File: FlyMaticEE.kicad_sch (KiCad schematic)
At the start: 1 part, among them U1 RASPBERRY_PI_4B_4GB

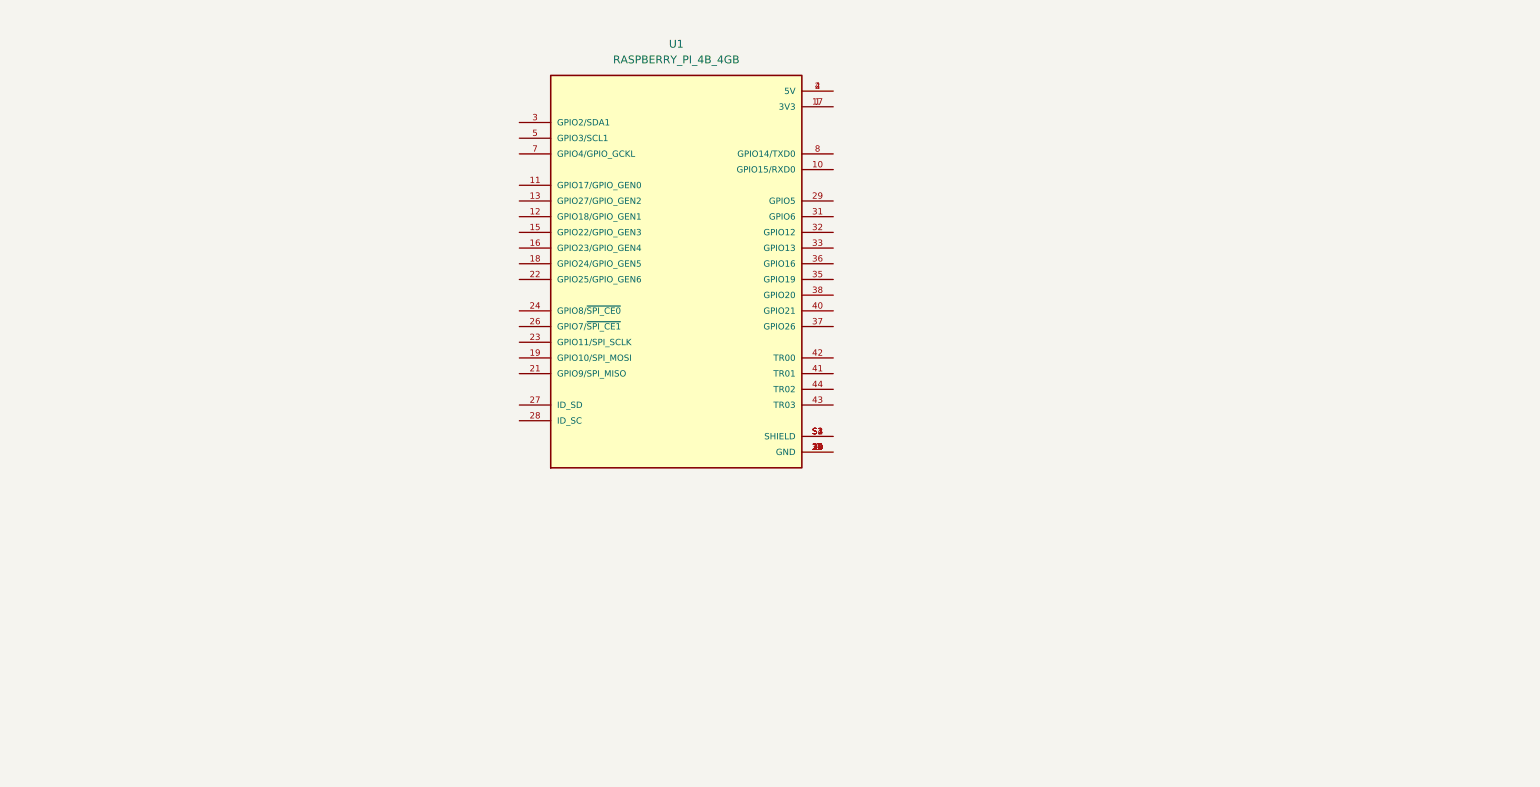
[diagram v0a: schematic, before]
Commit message: Add basic components to the schematic
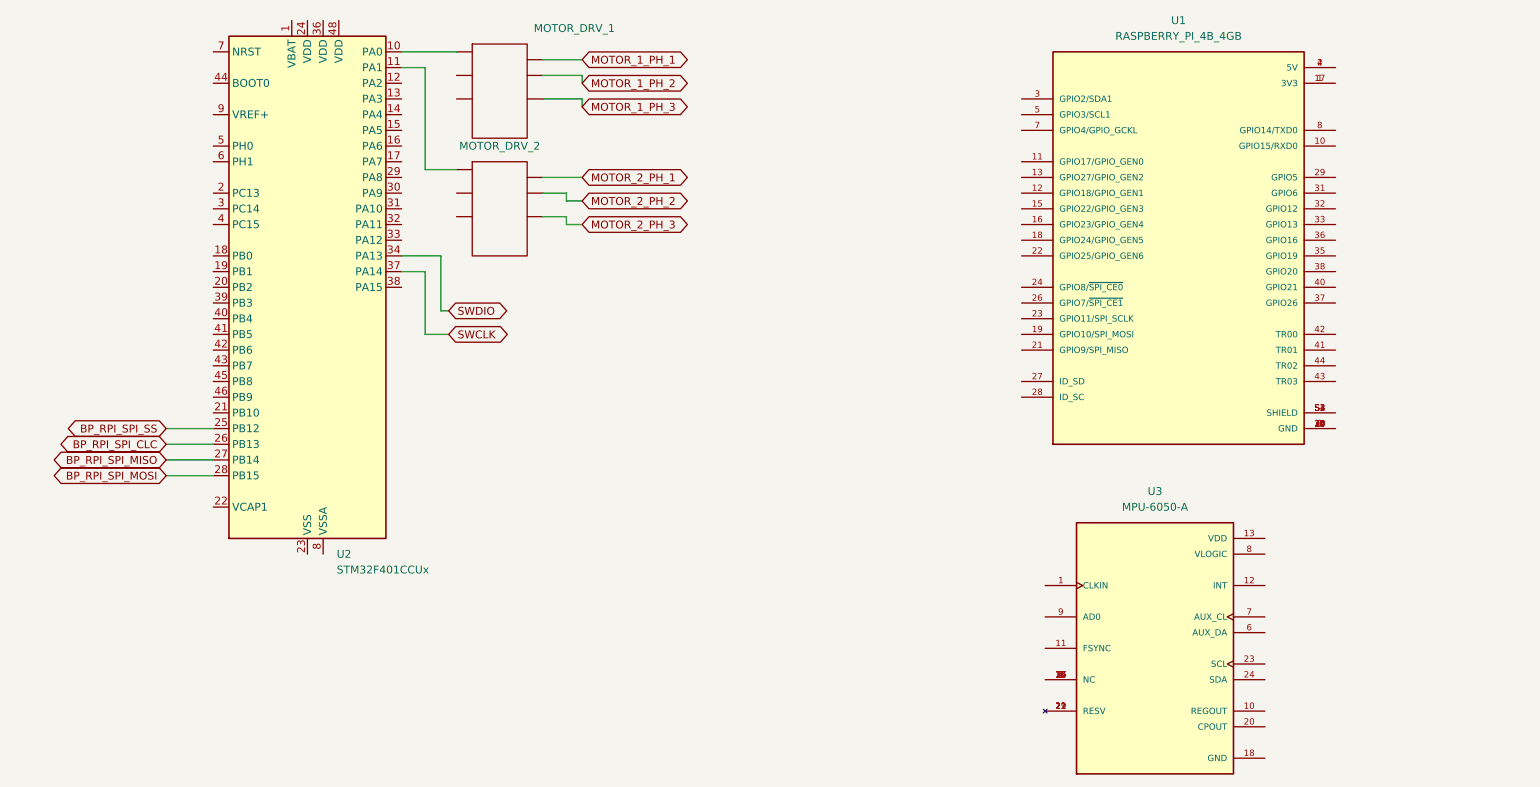
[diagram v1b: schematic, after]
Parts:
- added MOTOR_DRV_1, MOTOR_DRV_2: ~, symbol Driver_Motor:Brushless_ESC_20A_2-3S
- added U2: STM32F401CCUx, Package_DFN_QFN:QFN-48-1EP_7x7mm_P0.5mm_EP5.6x5.6mm, symbol MCU_ST_STM32F4:STM32F401CCUx
- added U3: MPU-6050-A, MPU-6050-A:QFN50P400X400X95-24N, symbol MPU-6050-A:MPU-6050-A
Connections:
- new net: U3.14 (NC), U3.15 (NC), U3.16 (NC), U3.17 (NC), U3.2 (NC), U3.3 (NC), U3.4 (NC), U3.5 (NC)
- new net: U3.19 (RESV), U3.21 (RESV), U3.22 (RESV)
- new net: MOTOR_DRV_1., U2.10 (PA0)
- new net: MOTOR_DRV_2., U2.11 (PA1)
- new net: U2.23 (VSS), U2.35 (VSS), U2.47 (VSS), U2.49 (VSS)
- new net BP_RPI_SPI_CLC: U2.26 (PB13)
- new net BP_RPI_SPI_MISO: U2.27 (PB14)
- new net BP_RPI_SPI_MOSI: U2.28 (PB15)
- new net BP_RPI_SPI_SS: U2.25 (PB12)
- new net MOTOR_1_PH_1: MOTOR_DRV_1.
- new net MOTOR_1_PH_2: MOTOR_DRV_1.
- new net MOTOR_1_PH_3: MOTOR_DRV_1.
- new net MOTOR_2_PH_1: MOTOR_DRV_2.
- new net MOTOR_2_PH_2: MOTOR_DRV_2.
- new net MOTOR_2_PH_3: MOTOR_DRV_2.
- new net SWCLK: U2.37 (PA14)
- new net SWDIO: U2.34 (PA13)
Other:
- moved on the sheet: U1

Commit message: Add pdf schematic to the project
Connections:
- net BP_RPI_SPI_CLC: now also U1.23 (GPIO11/SPI_SCLK)
- net BP_RPI_SPI_MISO: now also U1.21 (GPIO9/SPI_MISO)
- net BP_RPI_SPI_MOSI: now also U1.19 (GPIO10/SPI_MOSI)
- net BP_RPI_SPI_SS: now also U1.24 (GPIO8/~{SPI_CE0})
- net at U3.23 (SCL): now also U1.5 (GPIO3/SCL1)
- net at U3.24 (SDA): now also U1.3 (GPIO2/SDA1)
- net at U1.1 (3V3): no longer U1.17 (3V3)
- net at U1.2 (5V): no longer U1.4 (5V)
- net at U1.S2 (SHIELD), U1.S3 (SHIELD), U1.S4 (SHIELD): no longer U1.S1 (SHIELD)
- now unconnected: U1.14 (GND), U1.20 (GND), U1.25 (GND), U1.30 (GND), U1.34 (GND), U1.39 (GND), U1.6 (GND), U1.9 (GND)
- no-connect marks 0 -> 24
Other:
- moved on the sheet: MOTOR_DRV_1, MOTOR_DRV_2, U2, U3
